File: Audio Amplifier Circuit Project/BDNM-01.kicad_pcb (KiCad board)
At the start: 2 copper layers, 130.5 x 103 mm, 22 parts, among them J2 Power In, J3 Audio Out, J4 Audio In, Q1 2SC5200, Q2 2SC5200, Q3 MJE340, Q4 BC556

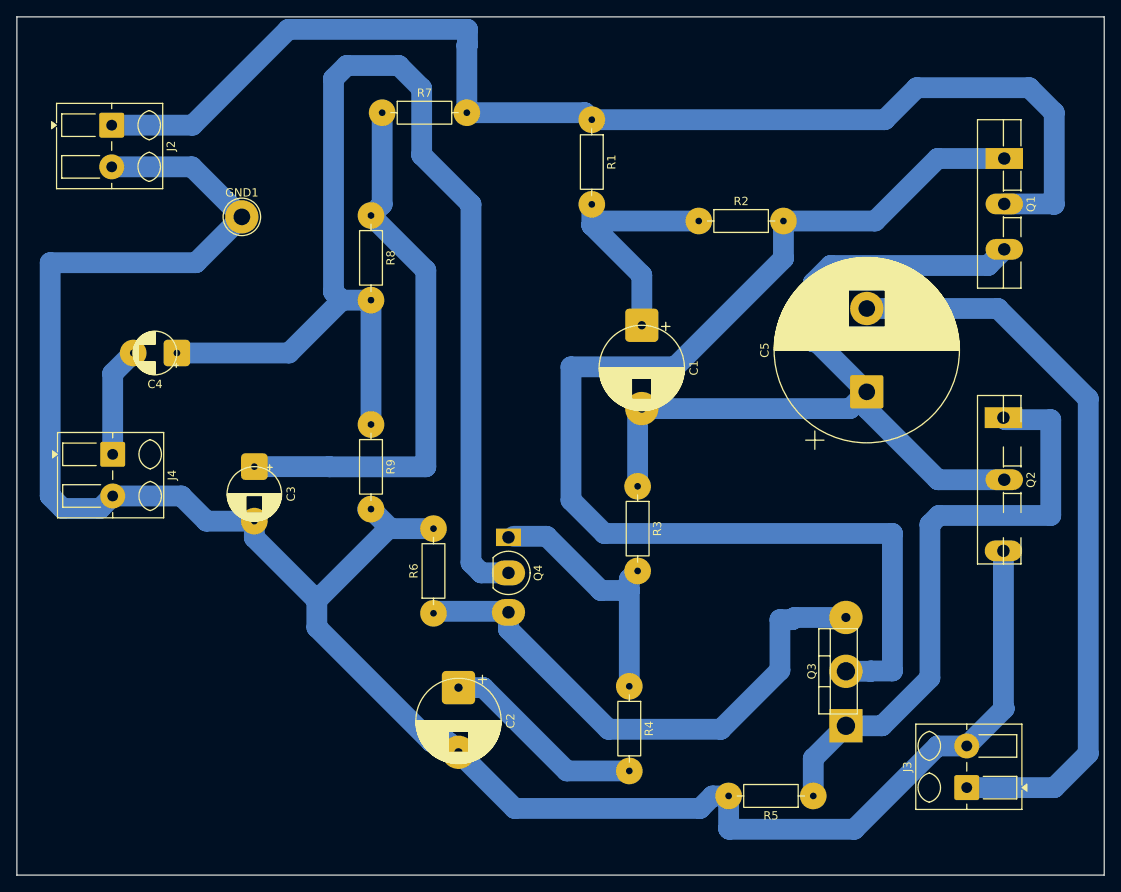
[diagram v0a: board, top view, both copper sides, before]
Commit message: gcode for audio amp board
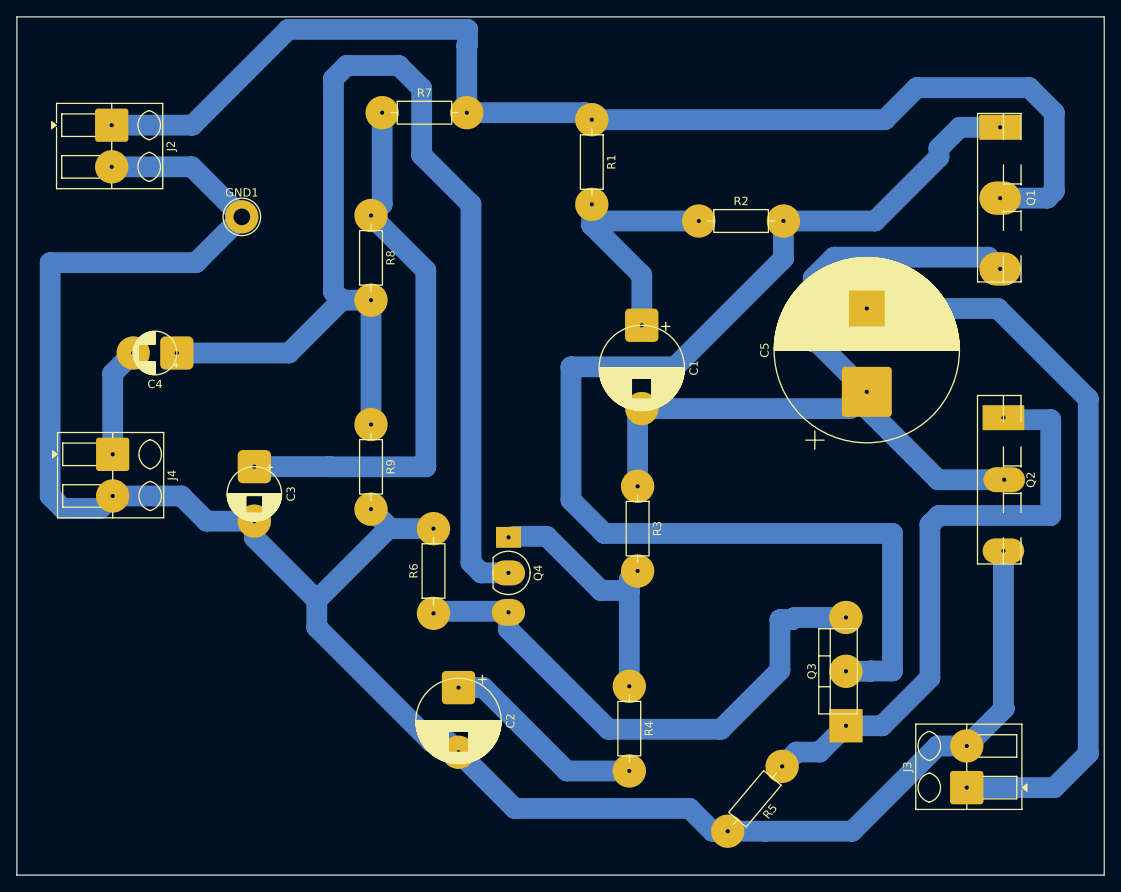
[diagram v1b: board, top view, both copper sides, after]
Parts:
- moved R5 5.15 mm to (94.3, 91.6), turned to -130 degrees
- moved Q1 0.75 mm to (120.9, 17.9)
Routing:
- net GND: track 256.5 -> 253.2 mm
- net Net-(Q1-B): track 143.3 -> 145.0 mm
- net Net-(Q1-E): track 100.0 -> 101.7 mm
- net Net-(J2-Pin_1): track 148.2 -> 147.4 mm
